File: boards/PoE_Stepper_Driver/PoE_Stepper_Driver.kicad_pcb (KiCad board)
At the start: 2 copper layers, 97.8 x 71.1 mm, 135 parts, among them J1 RJ45, J2 Motor, J3 Limits, J4 JTAG, J5 48V In, J6 12V, 3V3 Out, J7 PHY Data, J8 SPI Data, J9 UART, Q1 NMOS_POE, Q10 NMOS_POE, Q3 NMOS_POE, Q4 NMOS_POE, Q5 NMOS_POE, Q6 NMOS_POE, Q7 NMOS_POE, Q8 NMOS_POE, Q9 NMOS_POE, SW3 SW_Push, U1 LT4321, U14 DP83848C, U15 TMC429-I, U16 TMC2660C-PA, U2 LT4293, U3 STM32F407VETx, X1 SXO53C, Y1 8MHz

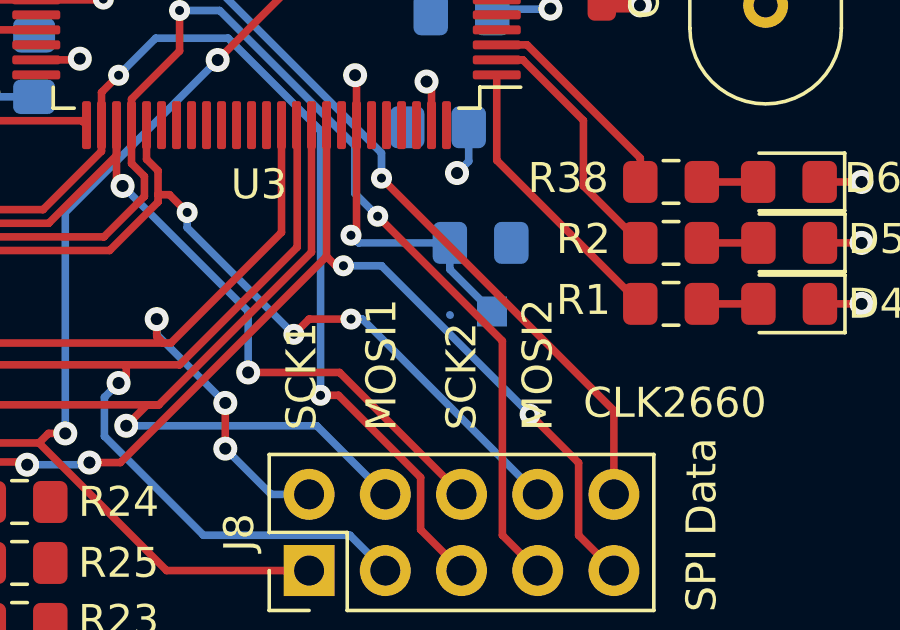
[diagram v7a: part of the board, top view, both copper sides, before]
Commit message: fixed weird track
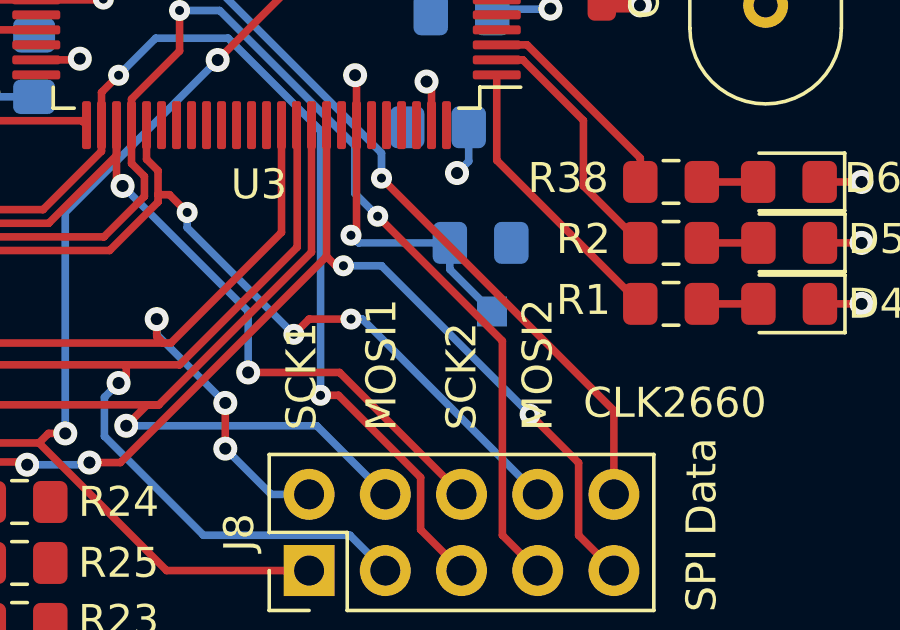
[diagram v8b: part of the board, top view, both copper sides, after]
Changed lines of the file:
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@@
     (thickness 1.6)
     (drawings 8)
-    (tracks 1413)
+    (tracks 1412)
     (zones 0)
     (modules 135)
@@
   (segment (start 170.236115 103.549485) (end 170.188901 103.502271) (width 0.254) (layer F.Cu) (net 196))
   (segment (start 170.236115 105.166967) (end 170.236115 103.549485) (width 0.254) (layer F.Cu) (net 196))
-  (segment (start 173.346 111.489934) (end 173.358533 111.502467) (width 0.254) (layer B.Cu) (net 196))
   (via (at 170.053 108.839) (size 0.7) (drill 0.3) (layers F.Cu B.Cu) (net 196))
   (segment (start 170.307 109.093) (end 170.053 108.839) (width 0.254) (layer B.Cu) (net 196))
